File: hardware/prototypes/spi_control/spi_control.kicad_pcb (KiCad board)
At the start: 4 copper layers, 66.9 x 43.2 mm, 85 parts, among them J1 USB_B_Micro, J39 Versa_1, J40 Versa_2, U1 ST1L08SPU33R, U2 MCP2210-I_MQ, U3 ADAR7251, U4 BGT24_Module, Y1 12MHZ, Y2 40MHz

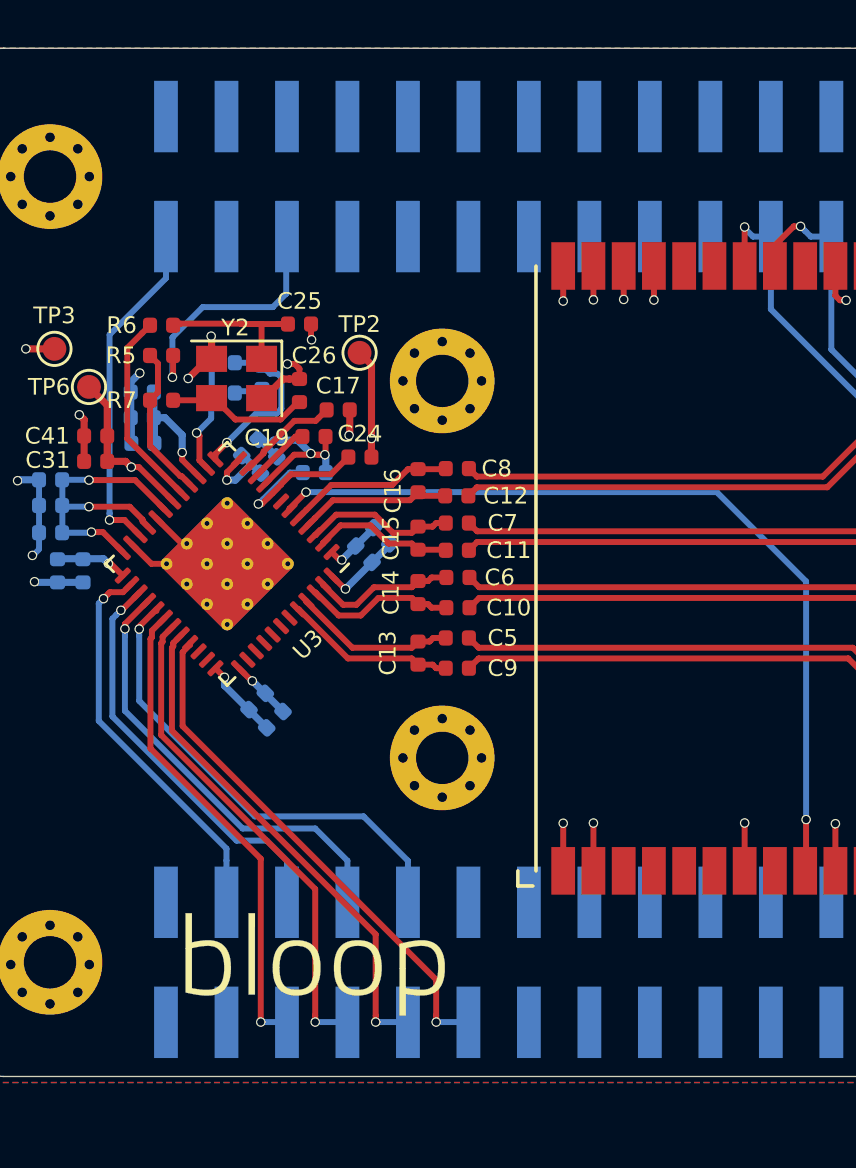
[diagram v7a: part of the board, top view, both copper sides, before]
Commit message: Optimized ADC bit routing, moved nets around for J39.
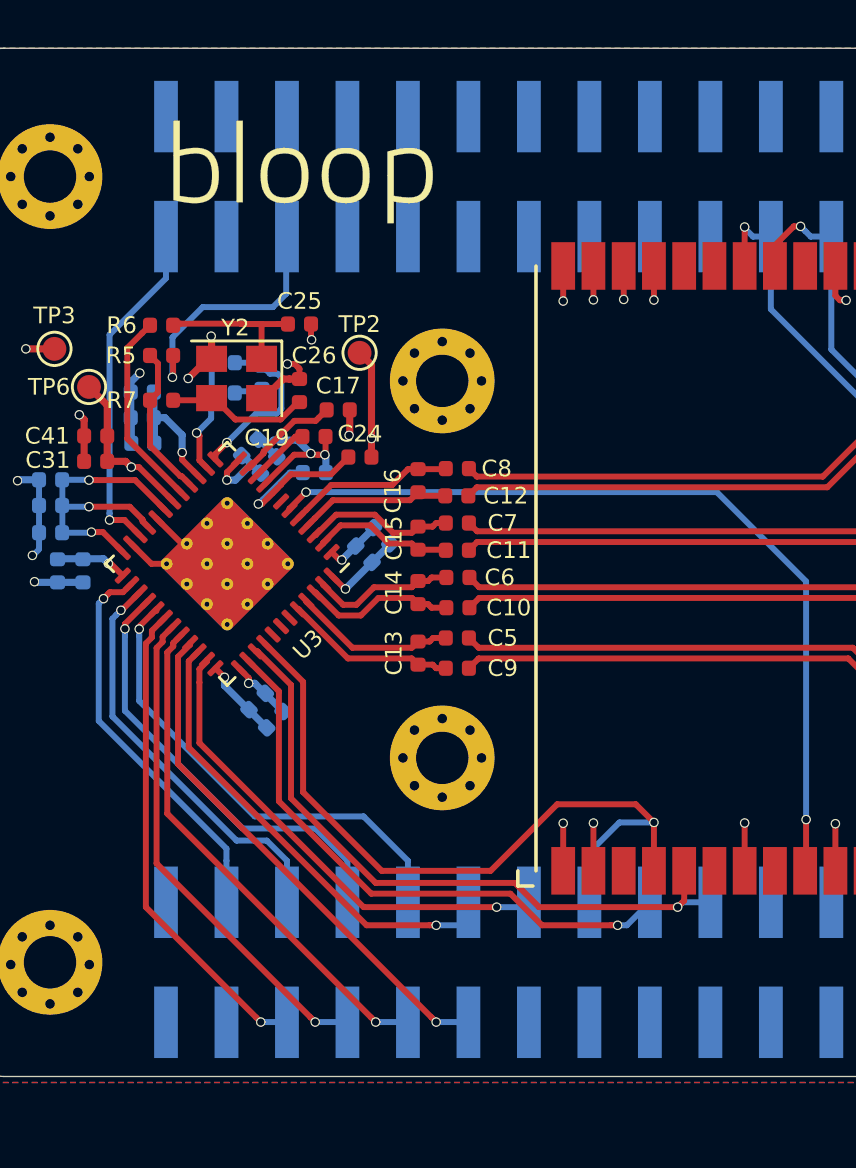
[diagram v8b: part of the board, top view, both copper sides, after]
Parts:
- moved ~ 33.3 mm to (71.6, 59.9)
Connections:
- J39 pad 12: /MISO -> /SCLK_ADC
- J39 pad 14: /MOSI -> /~CONV_START
- J39 pad 18: /SCLK_ADC -> /MISO
- J39 pad 20: Net-(J39-Pad20) -> /MOSI
- J39 pad 29: /~CONV_START -> Net-(J39-Pad29)
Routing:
- net /SCK: track 0.00 -> 31.9 mm, vias 0 -> 1
- net /MOSI: track 0.00 -> 28.0 mm, vias 0 -> 1
- net /MISO: track 0.00 -> 24.6 mm, vias 0 -> 1
- net /~CONV_START: track 0.00 -> 20.4 mm, vias 0 -> 1
- net /SCLK_ADC: track 0.00 -> 19.2 mm, vias 0 -> 1
